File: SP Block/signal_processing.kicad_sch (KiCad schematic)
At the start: 17 parts, among them U3 OPA365xxD, U6 OPA365xxD

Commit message: Refactor and polishing
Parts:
- added C32: 100n, symbol Device:C
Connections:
- net +5V: now also C32.1
- net GND: now also C32.2
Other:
- note added: "5Vpp- capable"
- note added: "C0G"
- note added: "X7R 50V"
- note added: "X7R OPA IN+"
- note added: "X7R OPA V+"
- note added: "floating (+/-) 2.5"
- note added: "over zero"
- note removed: "1.25Vpp"
- note removed: "??"
- note removed: "Ceramic"
- note removed: "Electrolytic"

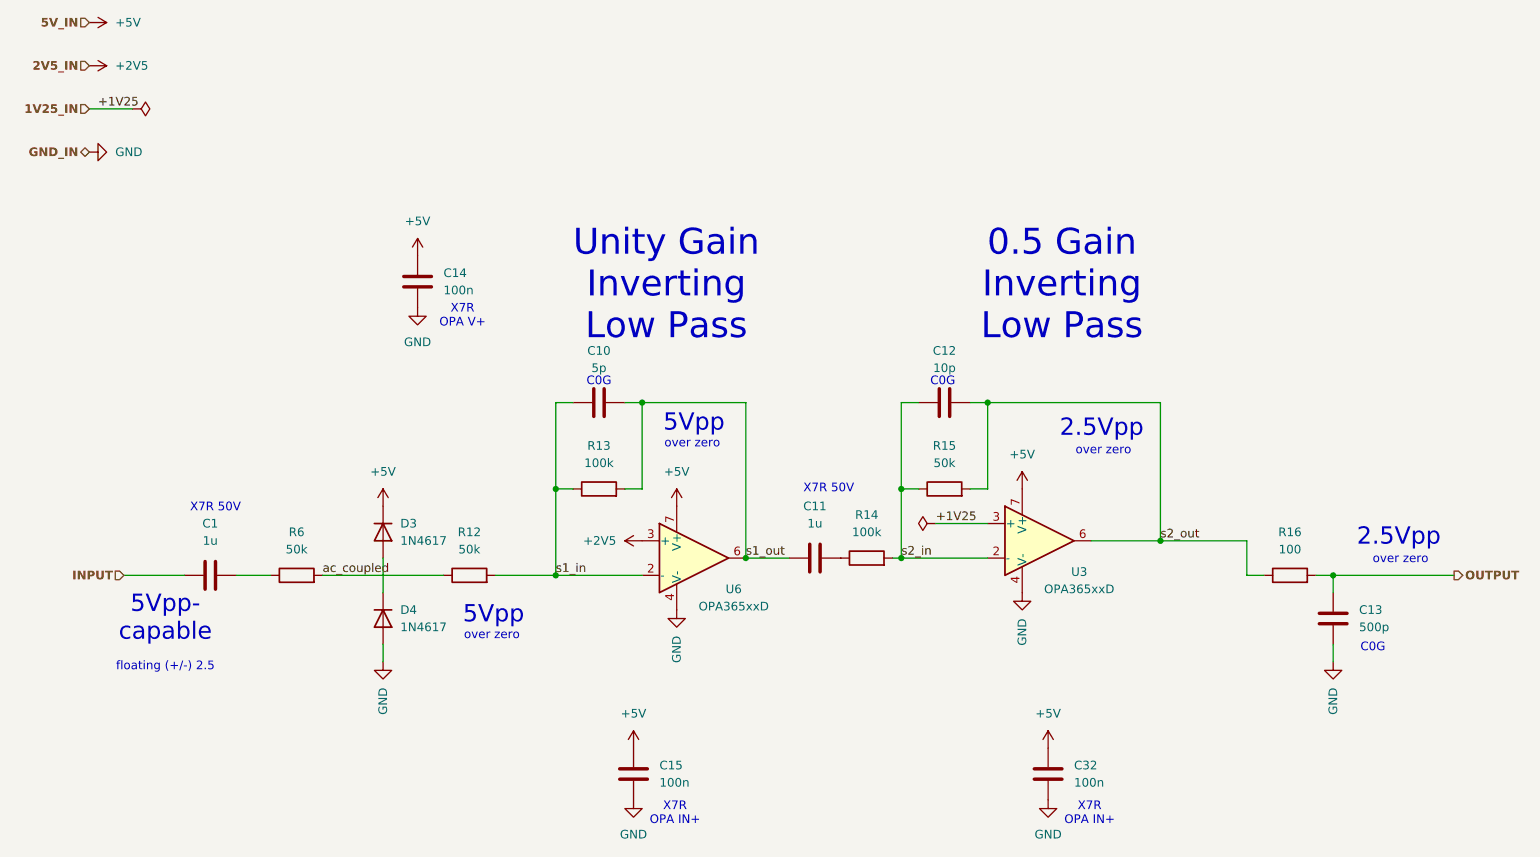
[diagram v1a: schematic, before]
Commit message: updated with available part sizes
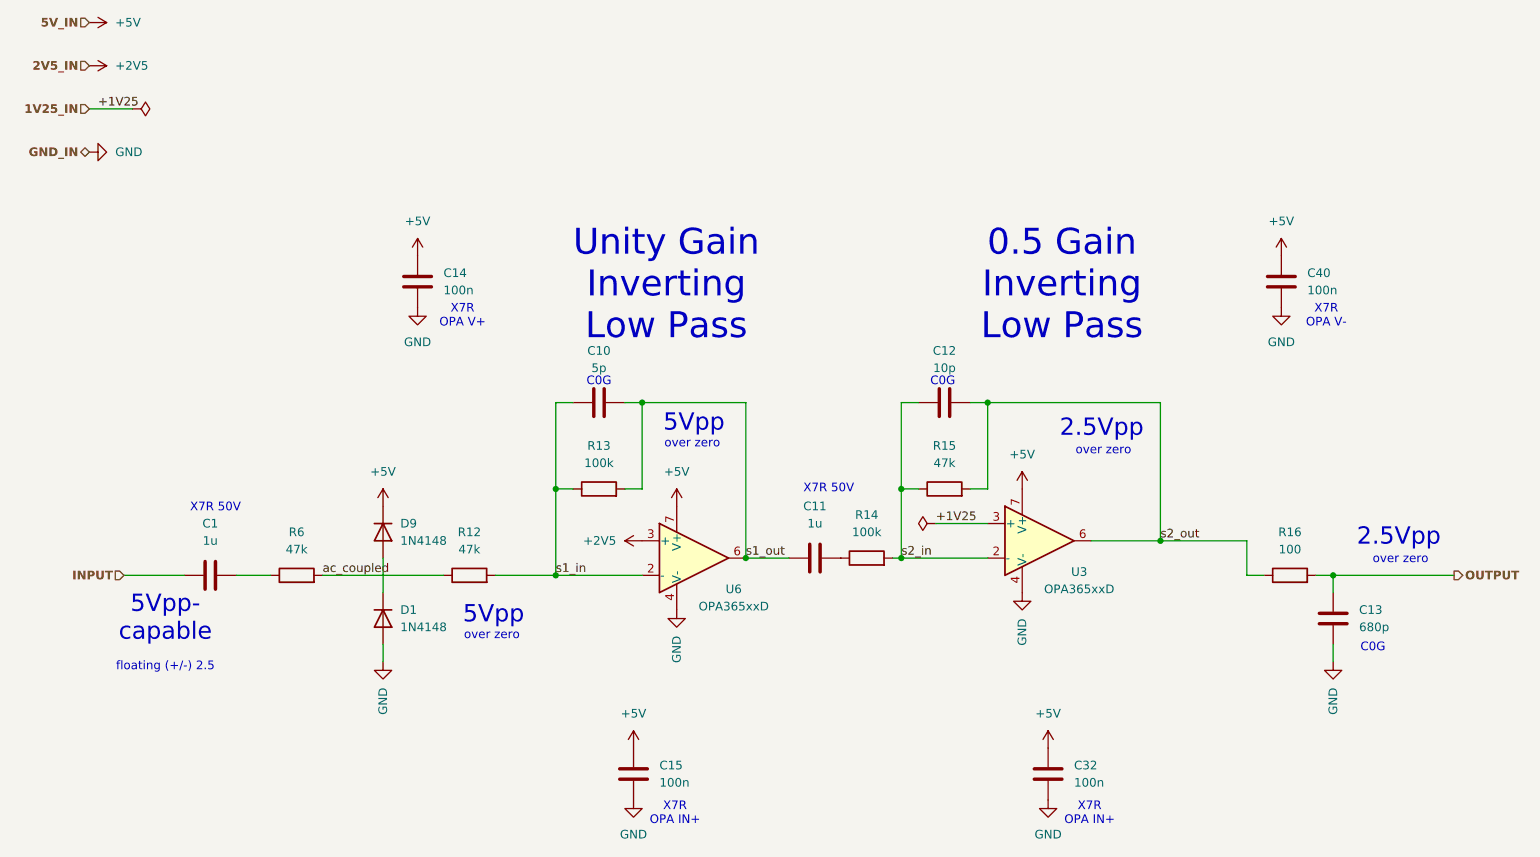
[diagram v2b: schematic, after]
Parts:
- removed D3, D4: 1N4617, symbol Device:D
- added C40: 100n, symbol Device:C
- added D1, D9: 1N4148, Diode_THT:D_DO-35_SOD27_P7.62mm_Horizontal, symbol Diode:1N4148
- C13: value 500p -> 680p
- R12, R15, R6: value 50k -> 47k
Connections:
- net +5V: now also C40.1, D9.1 (K)
- net GND: now also C40.2, D1.2 (A)
- new net: D1.1 (K), D9.2 (A)
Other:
- note added: "X7R OPA V-"
